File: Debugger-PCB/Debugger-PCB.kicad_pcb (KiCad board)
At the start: 2 copper layers, 72.1 x 49.7 mm, 67 parts, among them J1 Conn_01x04, J2 USB_C_Receptacle_USB2.0, J3 Conn_01x04, J4 Conn_01x02, Q1 S8050, SW1 SW_Push, SW2 SW_Push, SW3 SW_Push, U1 HX9193, U2 CH340E, U3 HX9193, U4 TJA1051T-3, U5 STM32F407VETx, U6 REF3030, U7 XPT2046TS, U8 W25Q32JVSS, Y1 12M

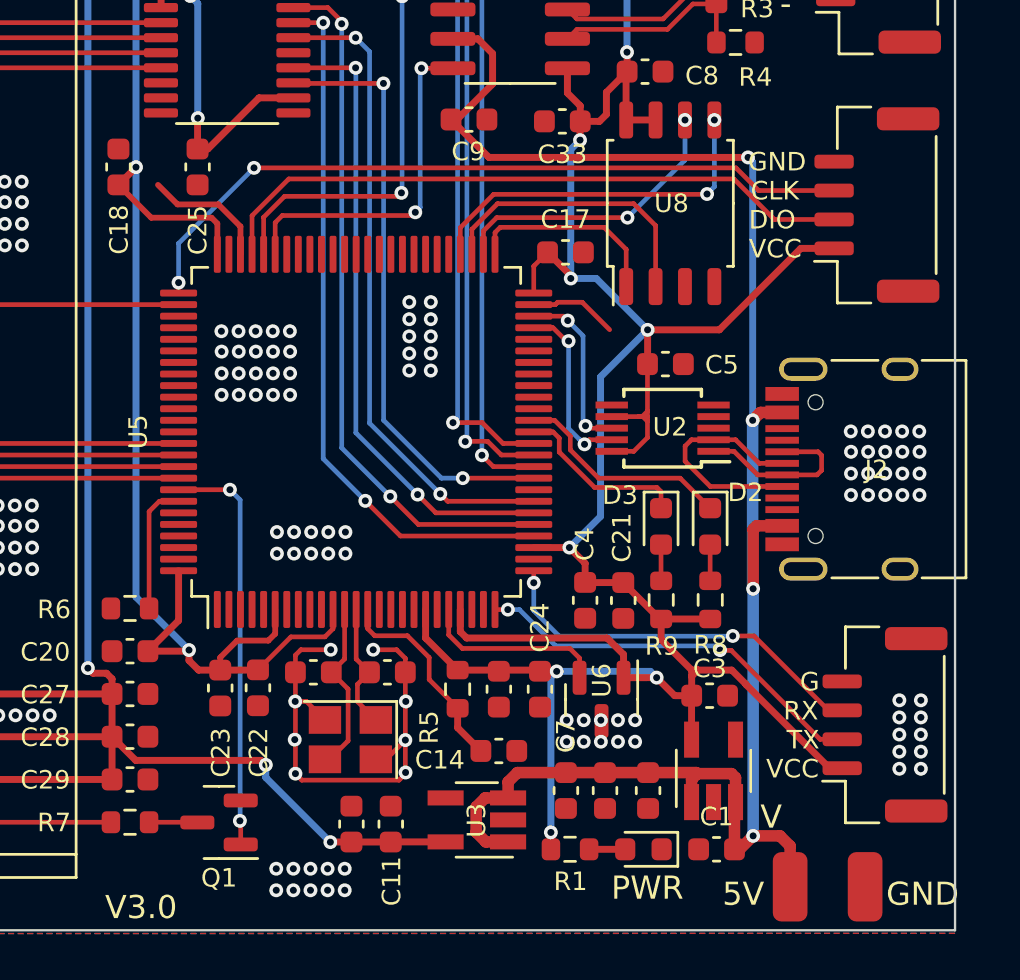
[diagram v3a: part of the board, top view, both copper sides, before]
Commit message: Add FreeRtos. Add fifo file from C board into support file folder. Using fifo to receive can datas. Creating data_processing file folder to sort the file of processing data. (All the changes are in debugger_code_f407 file folder.)
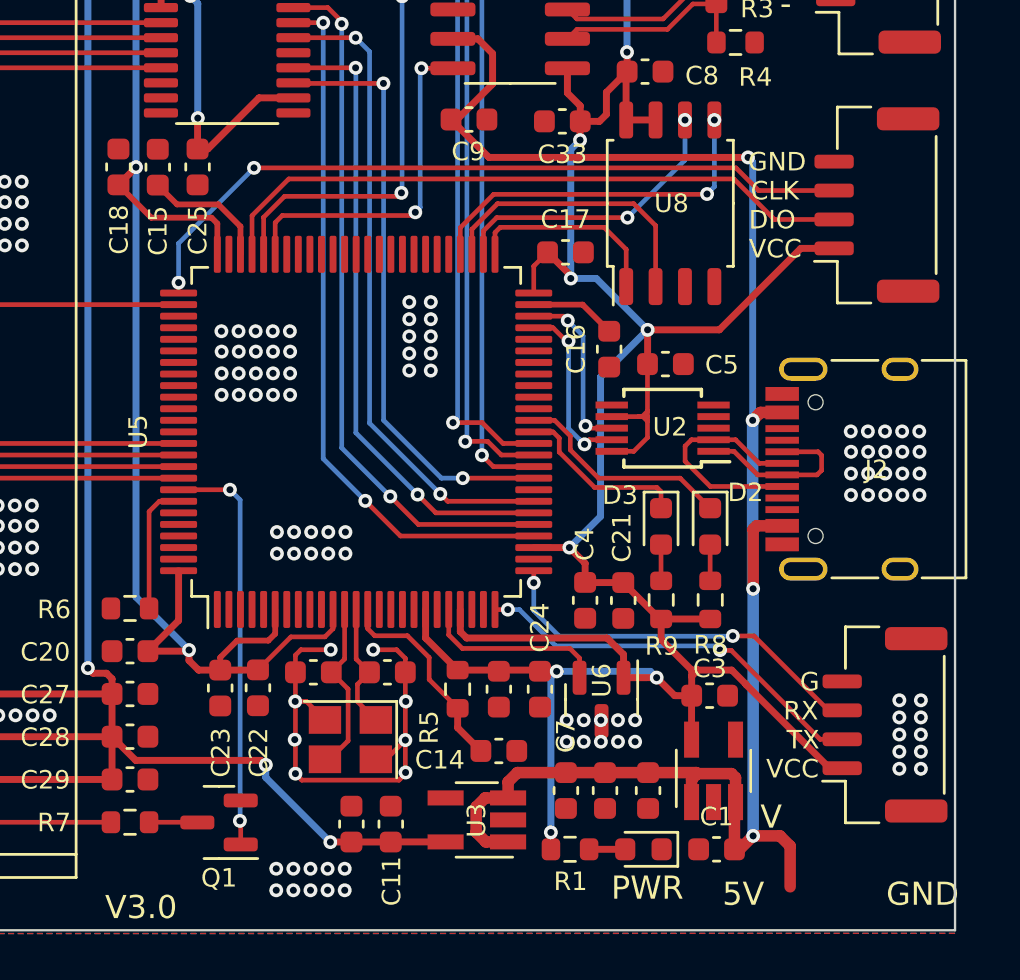
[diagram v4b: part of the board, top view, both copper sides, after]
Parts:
- removed ? (x2): , 
- added C15: 2.2u, Capacitor_SMD:C_0603_1608Metric, F.Cu at (154.6, 100.3)
- added C16: 2.2u, Capacitor_SMD:C_0603_1608Metric, F.Cu at (174.2, 108.1)
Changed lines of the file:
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@@
     )
   )
+  (footprint "Capacitor_SMD:C_0603_1608Metric" (layer "F.Cu")
+    (at 174.15 108.135 90)
+    (descr "Capacitor SMD 0603 (1608 Metric), square (rectangular) end terminal, IPC_7351 nominal, (Body size source: IPC-SM-782 page 76, https://www.pcb-3d.com/wordpress/wp-content/uploads/ipc-sm-782a_amendment_1_and_2.pdf), generated with kicad-footprint-generator")
+    (tags "capacitor")
+    (property "Sheetfile" "MCU.kicad_sch")
+    (property "Sheetname" "MCU")
+    (property "ki_description" "Unpolarized capacitor")
+    (property "ki_keywords" "cap capacitor")
+    (attr smd)
+    (fp_text reference "C16" (at 0 -1.43 90) (layer "F.SilkS")
+        (effects (font (size 0.8 0.8) (thickness 0.15)))
+    )
+    (fp_text value "2.2u" (at 0 1.43 90) (layer "F.Fab")
+        (effects (font (size 1 1) (thickness 0.15)))
+    )
+    (fp_text user "${REFERENCE}" (at 0 0 90) (layer "F.Fab")
+        (effects (font (size 0.4 0.4) (thickness 0.06)))
+    )
+    (fp_line (start -0.14058 -0.51) (end 0.14058 -0.51)
+      (stroke (width 0.12) (type solid)) (layer "F.SilkS"))
+    (fp_line (start -0.14058 0.51) (end 0.14058 0.51)
+      (stroke (width 0.12) (type solid)) (layer "F.SilkS"))
+    (fp_line (start -1.48 -0.73) (end 1.48 -0.73)
+      (stroke (width 0.05) (type solid)) (layer "F.CrtYd"))
+    (fp_line (start -1.48 0.73) (end -1.48 -0.73)
+      (stroke (width 0.05) (type solid)) (layer "F.CrtYd"))
+    (fp_line (start 1.48 -0.73) (end 1.48 0.73)
+      (stroke (width 0.05) (type solid)) (layer "F.CrtYd"))
+    (fp_line (start 1.48 0.73) (end -1.48 0.73)
+      (stroke (width 0.05) (type solid)) (layer "F.CrtYd"))
+    (fp_line (start -0.8 -0.4) (end 0.8 -0.4)
+      (stroke (width 0.1) (type solid)) (layer "F.Fab"))
+    (fp_line (start -0.8 0.4) (end -0.8 -0.4)
+      (stroke (width 0.1) (type solid)) (layer "F.Fab"))
+    (fp_line (start 0.8 -0.4) (end 0.8 0.4)
+      (stroke (width 0.1) (type solid)) (layer "F.Fab"))
+    (fp_line (start 0.8 0.4) (end -0.8 0.4)
+      (stroke (width 0.1) (type solid)) (layer "F.Fab"))
+    (pad "1" smd roundrect (at -0.775 0 90) (size 0.9 0.95) (layers "F.Cu" "F.Paste" "F.Mask") (roundrect_rratio 0.25)
+      (net 2 "GND") (pintype "passive"))
+    (pad "2" smd roundrect (at 0.775 0 90) (size 0.9 0.95) (layers "F.Cu" "F.Paste" "F.Mask") (roundrect_rratio 0.25)
+      (net 10 "Net-(U5-VCAP_1)") (pintype "passive"))
+    (model "${KICAD6_3DMODEL_DIR}/Capacitor_SMD.3dshapes/C_0603_1608Metric.wrl"
+      (offset (xyz 0 0 0))
+      (scale (xyz 1 1 1))
+      (rotate (xyz 0 0 0))
+    )
+  )
   (footprint "LED_SMD:LED_0603_1608Metric" (layer "F.Cu")
     (at 175.63 129.75 180)
@@
     )
   )
-  (footprint "" (layer "F.Cu")
-    (at 181.97 131.37)
-    (fp_text reference "" (at 0 0) (layer "F.SilkS")
-        (effects (font (size 1.27 1.27) (thickness 0.15)))
-    )
-    (fp_text value "" (at 0 0) (layer "F.SilkS")
-        (effects (font (size 1.27 1.27) (thickness 0.15)))
-    )
-    (pad "2" smd roundrect (at 0 0) (size 1.5 3) (layers "F.Cu" "F.Paste" "F.Mask") (roundrect_rratio 0.25)
-      (net 1 "+5V") (pinfunction "Pin_2") (pintype "passive"))
-  )
   (footprint "Capacitor_SMD:C_0603_1608Metric" (layer "F.Cu")
     (at 165.495 88.16 180)
@@
     )
   )
-  (footprint "" (layer "F.Cu")
-    (at 185.21 131.37)
-    (fp_text reference "" (at 0 0) (layer "F.SilkS")
-        (effects (font (size 1.27 1.27) (thickness 0.15)))
-    )
-    (fp_text value "" (at 0 0) (layer "F.SilkS")
-        (effects (font (size 1.27 1.27) (thickness 0.15)))
-    )
-    (pad "1" smd roundrect (at 0 0) (size 1.5 3) (layers "F.Cu" "F.Paste" "F.Mask") (roundrect_rratio 0.25)
-      (net 2 "GND") (pinfunction "Pin_1") (pintype "passive"))
-  )
   (footprint "Package_TO_SOT_SMD:SOT-23-5_HandSoldering" (layer "F.Cu")
     (at 168.43 128.48 180)
@@
   )
   (footprint "Capacitor_SMD:C_0603_1608Metric" (layer "F.Cu")
+    (at 154.64 100.27 -90)
+    (descr "Capacitor SMD 0603 (1608 Metric), square (rectangular) end terminal, IPC_7351 nominal, (Body size source: IPC-SM-782 page 76, https://www.pcb-3d.com/wordpress/wp-content/uploads/ipc-sm-782a_amendment_1_and_2.pdf), generated with kicad-footprint-generator")
+    (tags "capacitor")
+    (property "Sheetfile" "MCU.kicad_sch")
+    (property "Sheetname" "MCU")
+    (property "ki_description" "Unpolarized capacitor")
+    (property "ki_keywords" "cap capacitor")
+    (attr smd)
+    (fp_text reference "C15" (at 2.75 -0.01 90) (layer "F.SilkS")
+        (effects (font (size 0.8 0.8) (thickness 0.15)))
+    )
+    (fp_text value "2.2u" (at 0 1.43 90) (layer "F.Fab")
+        (effects (font (size 1 1) (thickness 0.15)))
+    )
+    (fp_text user "${REFERENCE}" (at 0 0 90) (layer "F.Fab")
+        (effects (font (size 0.4 0.4) (thickness 0.06)))
+    )
+    (fp_line (start -0.14058 -0.51) (end 0.14058 -0.51)
+      (stroke (width 0.12) (type solid)) (layer "F.SilkS"))
+    (fp_line (start -0.14058 0.51) (end 0.14058 0.51)
+      (stroke (width 0.12) (type solid)) (layer "F.SilkS"))
+    (fp_line (start -1.48 -0.73) (end 1.48 -0.73)
+      (stroke (width 0.05) (type solid)) (layer "F.CrtYd"))
+    (fp_line (start -1.48 0.73) (end -1.48 -0.73)
+      (stroke (width 0.05) (type solid)) (layer "F.CrtYd"))
+    (fp_line (start 1.48 -0.73) (end 1.48 0.73)
+      (stroke (width 0.05) (type solid)) (layer "F.CrtYd"))
+    (fp_line (start 1.48 0.73) (end -1.48 0.73)
+      (stroke (width 0.05) (type solid)) (layer "F.CrtYd"))
+    (fp_line (start -0.8 -0.4) (end 0.8 -0.4)
+      (stroke (width 0.1) (type solid)) (layer "F.Fab"))
+    (fp_line (start -0.8 0.4) (end -0.8 -0.4)
+      (stroke (width 0.1) (type solid)) (layer "F.Fab"))
+    (fp_line (start 0.8 -0.4) (end 0.8 0.4)
+      (stroke (width 0.1) (type solid)) (layer "F.Fab"))
+    (fp_line (start 0.8 0.4) (end -0.8 0.4)
+      (stroke (width 0.1) (type solid)) (layer "F.Fab"))
+    (pad "1" smd roundrect (at -0.775 0 270) (size 0.9 0.95) (layers "F.Cu" "F.Paste" "F.Mask") (roundrect_rratio 0.25)
+      (net 2 "GND") (pintype "passive"))
+    (pad "2" smd roundrect (at 0.775 0 270) (size 0.9 0.95) (layers "F.Cu" "F.Paste" "F.Mask") (roundrect_rratio 0.25)
+      (net 9 "Net-(U5-VCAP_2)") (pintype "passive"))
+    (model "${KICAD6_3DMODEL_DIR}/Capacitor_SMD.3dshapes/C_0603_1608Metric.wrl"
+      (offset (xyz 0 0 0))
+      (scale (xyz 1 1 1))
+      (rotate (xyz 0 0 0))
+    )
+  )
+  (footprint "Capacitor_SMD:C_0603_1608Metric" (layer "F.Cu")
     (at 173.97 127.21 -90)
     (descr "Capacitor SMD 0603 (1608 Metric), square (rectangular) end terminal, IPC_7351 nominal, (Body size source: IPC-SM-782 page 76, https://www.pcb-3d.com/wordpress/wp-content/uploads/ipc-sm-782a_amendment_1_and_2.pdf), generated with kicad-footprint-generator")
@@
   (segment (start 170.89 111.21) (end 171.792803 111.21) (width 0.2032) (layer "F.Cu") (net 8))
   (segment (start 173.6902 113.7102) (end 177.2162 113.7102) (width 0.2032) (layer "F.Cu") (net 8))
-  (segment (start 155.495 101.88) (end 157.26 101.88) (width 0.25) (layer "F.Cu") (net 9))
-  (segment (start 154.65 101.035) (end 155.495 101.88) (width 0.25) (layer "F.Cu") (net 9))
-  (segment (start 158.215 102.835) (end 158.215 104.035) (width 0.25) (layer "F.Cu") (net 9))
-  (segment (start 157.26 101.88) (end 158.215 102.835) (width 0.25) (layer "F.Cu") (net 9))
-  (segment (start 170.89 106.21) (end 171.819209 106.21) (width 0.2032) (layer "F.Cu") (net 10))
-  (segment (start 171.920809 106.1084) (end 172.9834 106.1084) (width 0.2032) (layer "F.Cu") (net 10))
-  (segment (start 171.819209 106.21) (end 171.920809 106.1084) (width 0.2032) (layer "F.Cu") (net 10))
-  (segment (start 172.9834 106.1084) (end 174.17 107.295) (width 0.2032) (layer "F.Cu") (net 10))
+  (segment (start 155.475 101.88) (end 154.64 101.045) (width 0.25) (layer "F.Cu") (net 9))
+  (segment (start 157.26 101.88) (end 155.475 101.88) (width 0.25) (layer "F.Cu") (net 9))
+  (segment (start 158.215 104.035) (end 158.215 102.835) (width 0.25) (layer "F.Cu") (net 9))
+  (segment (start 158.215 102.835) (end 157.26 101.88) (width 0.25) (layer "F.Cu") (net 9))
+  (segment (start 170.89 106.21) (end 173 106.21) (width 0.25) (layer "F.Cu") (net 10))
+  (segment (start 173 106.21) (end 174.15 107.36) (width 0.25) (layer "F.Cu") (net 10))
   (segment (start 176.39 114.29) (end 176.39 115.007) (width 0.2032) (layer "F.Cu") (net 11))
   (segment (start 176.2134 114.1134) (end 176.39 114.29) (width 0.2032) (layer "F.Cu") (net 11))
@@
       )
     )
-  )
-  (zone (net 10) (net_name "Net-(U5-VCAP_1)") (layer "F.Cu") (name "$teardrop_padvia$") (hatch edge 0.5)
-    (priority 30271)
-    (attr (teardrop (type padvia)))
-    (connect_pads yes (clearance 0))
-    (min_thickness 0.0254) (filled_areas_thickness no)
-    (fill yes (thermal_gap 0.5) (thermal_bridge_width 0.5) (island_removal_mode 1) (island_area_min 10))
-    (polygon
-      (pts
-        (xy 171.905752 106.26714)
-        (xy 171.762069 106.123457)
-        (xy 171.643701 106.065709)
-        (xy 170.889293 106.210707)
-        (xy 171.652705 106.348274)
-      )
-    )

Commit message: temp.change the PCB.And change the code.
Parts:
- removed C25, C26, C27, C28, C29: 100n, Capacitor_SMD:C_0603_1608Metric
- removed LCD1: 1.8inch-TFT-LCD, debugger:TFT-LCD1.8inch
- removed R4: 10k, Resistor_SMD:R_0603_1608Metric
- added C34: 4.7u, Capacitor_SMD:C_0603_1608Metric, F.Cu at (178.5, 134.7)
- added C35: 100n, Capacitor_SMD:C_0603_1608Metric, F.Cu at (176.4, 134.7)
- added C36: 4.7u, Capacitor_SMD:C_0603_1608Metric, F.Cu at (169.9, 134.3)
- added C37: 100n, Capacitor_SMD:C_0603_1608Metric, F.Cu at (168.2, 134.3)
- added C38: 4.7u, Capacitor_SMD:C_0603_1608Metric, F.Cu at (129.2, 92.5)
- added C39: 100n, Capacitor_SMD:C_0603_1608Metric, F.Cu at (127.5, 92.6)
- added C40: 4.7u, Capacitor_SMD:C_0805_2012Metric, F.Cu at (121.0, 92.8)
- added C41: 100n, Capacitor_SMD:C_0805_2012Metric, F.Cu at (118.8, 92.8)
- added C42: 100n, Capacitor_SMD:C_0603_1608Metric, F.Cu at (123.8, 101.6)
- added C43: 103, Capacitor_SMD:C_0603_1608Metric, F.Cu at (127.1, 104.2)
- added C44: 101, Capacitor_SMD:C_0603_1608Metric, F.Cu at (129.3, 96.5)
- added C45: 22uf 0603, Capacitor_SMD:C_1206_3216Metric, F.Cu at (130.6, 102.6)
- added C46: 104, Capacitor_SMD:C_0603_1608Metric, F.Cu at (132.7, 103.3)
- added D4: LED, LED_SMD:LED_0603_1608Metric, F.Cu at (174.3, 130.8)
- added D5: , LED_SMD:LED_0603_1608Metric, F.Cu at (128.0, 136.5)
- added D6: , LED_SMD:LED_0603_1608Metric, F.Cu at (130.6, 136.5)
- added D7: , LED_SMD:LED_0603_1608Metric, F.Cu at (133.2, 136.5)
- added D8: , LED_SMD:LED_0603_1608Metric, F.Cu at (124.0, 120.9)
- added D9: LED, LED_SMD:LED_0603_1608Metric, F.Cu at (117.4, 88.2)
- added H2: MountingHole, ic:mo, F.Cu at (141.5, 130.7)
- added J5: Conn_01x02, Connector_PinHeader_2.54mm:PinHeader_1x02_P2.54mm_Vertical, F.Cu at (111.9, 119.8)
- added J6: Conn_01x14, Connector_FFC-FPC:Hirose_FH12-14S-0.5SH_1x14-1MP_P0.50mm_Horizontal, F.Cu at (155.3, 133.8)
- added J7: axt430124, Connector_PinHeader_1.27mm:PinHeader_2x15_P1.27mm_Vertical, F.Cu at (138.8, 87.5)
- added J8: USB_C_Receptacle_USB2.0, Connector_USB:USB_C_Receptacle_HRO_TYPE-C-31-M-12, F.Cu at (114.1, 110.9)
- added J9: Conn_01x02, Connector_PinHeader_2.54mm:PinHeader_1x02_P2.54mm_Vertical, F.Cu at (116.2, 101.6)
- added L1: 1u, PCM_008_GN_POWER-CHOKE_SMD:MC-0630, F.Cu at (134.7, 119.5)
- added L2: 600r, Inductor_SMD:L_0805_2012Metric, F.Cu at (119.5, 101.3)
- added L3: 2.2uh, Inductor_SMD_Wurth:L_Wurth_WE-LQSH-4020, F.Cu at (127.9, 107.6)
- added Q2: SI2301, Package_TO_SOT_SMD:SOT-23, F.Cu at (146.3, 135.5)
- added R13: 1K, Resistor_SMD:R_0603_1608Metric, F.Cu at (171.0, 131.0)
- added R14: 10k, Resistor_SMD:R_0603_1608Metric, F.Cu at (125.6, 132.9)
- added R15: 10k, Resistor_SMD:R_0603_1608Metric, F.Cu at (128.1, 132.9)
- added R16: 10k, Resistor_SMD:R_0603_1608Metric, F.Cu at (130.6, 132.9)
- added R17: 10k, Resistor_SMD:R_0603_1608Metric, F.Cu at (133.1, 132.9)
- added R18: 10k, Resistor_SMD:R_0603_1608Metric, F.Cu at (127.1, 122.2)
- added R19: 10k, Resistor_SMD:R_0603_1608Metric, F.Cu at (127.1, 120.1)
- added R20: 200K, Resistor_SMD:R_0603_1608Metric, F.Cu at (126.1, 98.2)
- added R21: 220K, Resistor_SMD:R_0603_1608Metric, F.Cu at (129.3, 98.1)
- added R22: 30k, Resistor_SMD:R_0603_1608Metric, F.Cu at (126.2, 96.5)
- added SW4: SW_SPDT, Button_Switch_SMD:SW_SPDT_PCM12, F.Cu at (112.1, 129.3)
- added U10: ~, Package_DFN_QFN:DFN-8-1EP_3x3mm_P0.65mm_EP1.55x2.4mm, F.Cu at (124.3, 92.8)
- added U9: ~, Package_DFN_QFN:DFN-8-1EP_3x3mm_P0.65mm_EP1.55x2.4mm, F.Cu at (173.2, 134.5)
- C1: value 10u -> 100n
- C10, C3: value 100n -> 22u; footprint Capacitor_SMD:C_0603_1608Metric -> Capacitor_SMD:C_1206_3216Metric
- C11: value 10u -> 106 1206; footprint Capacitor_SMD:C_0603_1608Metric -> Capacitor_SMD:C_1206_3216Metric
- C2: value 100n -> 10u; footprint Capacitor_SMD:C_0603_1608Metric -> Capacitor_SMD:C_1206_3216Metric
- C4, C6: value 10u -> 22u; footprint Capacitor_SMD:C_0603_1608Metric -> Capacitor_SMD:C_1206_3216Metric
- D1: value LED -> (none)
- H1: value mountinghole -> MountingHole; footprint MountingHole:MountingHole_2.1mm -> ic:mo
- Q1: value S8050 -> AO3407
- R1: value 1k -> 10K
- R2: value 10k -> 1K
- R7: value R -> 10k
- U1: value HX9193 -> IP5306; footprint Package_TO_SOT_SMD:SOT-23-5_HandSoldering -> PCM_004_GN_MIDDLE-SEMI_SMD:SOP-8EP_3949
- U3: value HX9193 -> SY8303; footprint Package_TO_SOT_SMD:SOT-23-5_HandSoldering -> PCM_003_GN_SMALL-SEMI_SMD:SOT-23-8
- U7: value XPT2046TS -> pesd1can; footprint debugger:TSSOP-16_4.4x5mm_P0.65mm -> PCM_003_GN_SMALL-SEMI_SMD:SOT-23
- moved H1 80.2 mm to (119.2, 130.6), turned to 90 degrees
- moved R2 63.7 mm to (115.9, 88.1), turned to -90 degrees
- moved C1 59.5 mm to (121.1, 115.3), turned to 90 degrees
- moved C7 58.1 mm to (114.7, 119.3)
- moved C2 57.1 mm to (121.1, 110.9)
- moved U1 53.3 mm to (126.3, 116.5), turned to 0 degrees
- moved C11 51.1 mm to (121.8, 100.9), turned to -90 degrees
- moved D1 50.6 mm to (125.5, 136.8), turned to 90 degrees
- moved U3 49.9 mm to (126.7, 101.1), turned to 90 degrees
- moved C3 41.9 mm to (137.9, 112.6), turned to 90 degrees
- moved Q1 40.2 mm to (118.2, 119.5), turned to 0 degrees
- moved C4 38.6 mm to (135.0, 112.6), turned to 90 degrees
- moved R7 37.8 mm to (116.1, 122.4)
- moved C6 36.2 mm to (140.8, 112.7), turned to 90 degrees
- moved C10 34.6 mm to (132.3, 112.6)
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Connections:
- net Net-(U5-NRST) renamed /MCU/RESET
- C1 pad 1: +5V -> GND
- C1 pad 2: GND -> BATE_5V
- C10 pad 1: LCD_3V3 -> +5V
- C10 pad 2: GND -> GND1
- C11 pad 1: LCD_3V3 -> GND
- C11 pad 2: GND -> Net-(U3-EN)
- C2 pad 1: +5V -> GND
- C2 pad 2: GND -> BATE_5V
- C3 pad 1: VCC -> +5V
- C3 pad 2: GND -> GND1
- C4 pad 1: VCC -> +5V
- C4 pad 2: GND -> GND1
- C6 pad 2: GND -> GND1
- C7 pad 1: +5V -> G
- D1 pad 1: GND -> Net-(D1-Cathode)
- D1 pad 2: Net-(D1-A) -> Net-(D1-Anode)
- Q1 pad 1: /MCU/LCD_LED -> G
- Q1 pad 2: GND -> /Power&Port/VBAT+
- Q1 pad 3: Net-(Q1-C) -> /Power&Port/VBAT
- R1 pad 1: VCC -> /MCU/LCD_LED
- R1 pad 2: Net-(D1-A) -> GND
- R2 pad 1: GND -> VCC
- R2 pad 2: /Power&Port/CAN+ -> Net-(D9-A)
- R7 pad 1: /TFT/LED- -> G
- R7 pad 2: Net-(Q1-C) -> /Power&Port/VBAT+
- U1 pad 1: +5V -> BATE_5V
- U1 pad 2: GND -> Net-(U1-LED1)
- U1 pad 3: +5V -> Net-(U1-LED2)
- U1 pad 4: unconnected-(U1-NC-Pad4) -> Net-(D1-Cathode)
- U1 pad 5: VCC -> Net-(U1-KEY)
- U3 pad 1: +5V -> Net-(U3-FB)
- U3 pad 2: GND -> Net-(U3-FS)
- U3 pad 3: +5V -> GND
- U3 pad 4: unconnected-(U3-NC-Pad4) -> GND
- U3 pad 5: LCD_3V3 -> Net-(U3-EN)
- U5 pad 15: unconnected-(U5-PC0-Pad15) -> /MCU/LCD_CS0
- U5 pad 16: unconnected-(U5-PC1-Pad16) -> /MCU/ADC1_IN11
- U5 pad 17: unconnected-(U5-PC2-Pad17) -> /MCU/ADC1_IN12
- U5 pad 18: unconnected-(U5-PC3-Pad18) -> /MCU/ADC1_IN13
- U5 pad 23: unconnected-(U5-PA0-Pad23) -> /MCU/ADC1_IN0
- U5 pad 24: unconnected-(U5-PA1-Pad24) -> /MCU/ADC1_IN1
- U5 pad 33: unconnected-(U5-PC4-Pad33) -> /MCU/ADC1_IN14
- U5 pad 40: unconnected-(U5-PE9-Pad40) -> /MCU/TIM1_CH1
- U5 pad 42: unconnected-(U5-PE11-Pad42) -> /MCU/TIM1_CH2
- U5 pad 56: unconnected-(U5-PD9-Pad56) -> /MCU/I2C3_SDA
- U5 pad 59: unconnected-(U5-PD12-Pad59) -> /MCU/TIM4_CH2
- U5 pad 60: unconnected-(U5-PD13-Pad60) -> /MCU/TIM4_CH1
- U5 pad 63: unconnected-(U5-PC6-Pad63) -> /MCU/TIM3_CH1
- U5 pad 64: unconnected-(U5-PC7-Pad64) -> /MCU/TIM3_CH2
- U5 pad 67: unconnected-(U5-PA8-Pad67) -> /MCU/I2C3_SCL
- U5 pad 68: unconnected-(U5-PA9-Pad68) -> /MCU/KEY5
- U5 pad 69: unconnected-(U5-PA10-Pad69) -> /MCU/KEY4
- U5 pad 95: unconnected-(U5-PB8-Pad95) -> /MCU/LCD_CS
- U5 pad 96: unconnected-(U5-PB9-Pad96) -> /MCU/LCD_DC
- U7 pad 1: LCD_3V3 -> /Power&Port/CAN+
- U7 pad 2: /TFT/T_XP -> /Power&Port/CAN-
- U7 pad 3: /TFT/T_YP -> GND
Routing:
- net VCC: track 196.2 -> 3.81 mm, vias 12 -> 0
- net LCD_3V3: track 138.2 -> 0.00 mm, vias 6 -> 0
- net +5V: track 78.0 -> 29.6 mm, vias 4 -> 2
- net /Key&LED/KEY1: track 41.6 -> 0.00 mm, vias 2 -> 0
- net /Key&LED/KEY3: track 37.6 -> 0.00 mm, vias 2 -> 0
- net /TFT/T_XP: track 36.8 -> 0.00 mm, vias 2 -> 0
- net /TFT/T_YP: track 36.0 -> 0.00 mm, vias 2 -> 0
- net /TFT/T_XM: track 35.5 -> 0.00 mm, vias 2 -> 0
- net /TFT/T_YM: track 34.8 -> 0.00 mm, vias 2 -> 0
- net /MCU/LCD_CS: track 33.9 -> 0.00 mm
- net /Key&LED/KEY2: track 33.7 -> 0.00 mm, vias 2 -> 0
- net /MCU/SWCLK: track 32.2 -> 0.00 mm, vias 2 -> 0
- net /MCU/TOUCH_CS: track 30.6 -> 0.00 mm, vias 2 -> 0
- net /MCU/TOUCH_CLK: track 30.4 -> 0.00 mm, vias 2 -> 0
- net /MCU/SWDIO: track 28.2 -> 0.00 mm
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- removed copper zone on B.Cu, net GND
- removed copper zone on F.Cu, net GND
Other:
- board size 72.1 x 49.7 mm -> 78.9 x 55 mm
- board text removed: "V"
